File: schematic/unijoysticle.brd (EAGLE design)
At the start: 88.6 x 45.7 mm, 8 parts, among them CN1 DC JACK, IC1 4066N, IC2 4066N, IC3 4066N, J1 DB9, J2 DB9

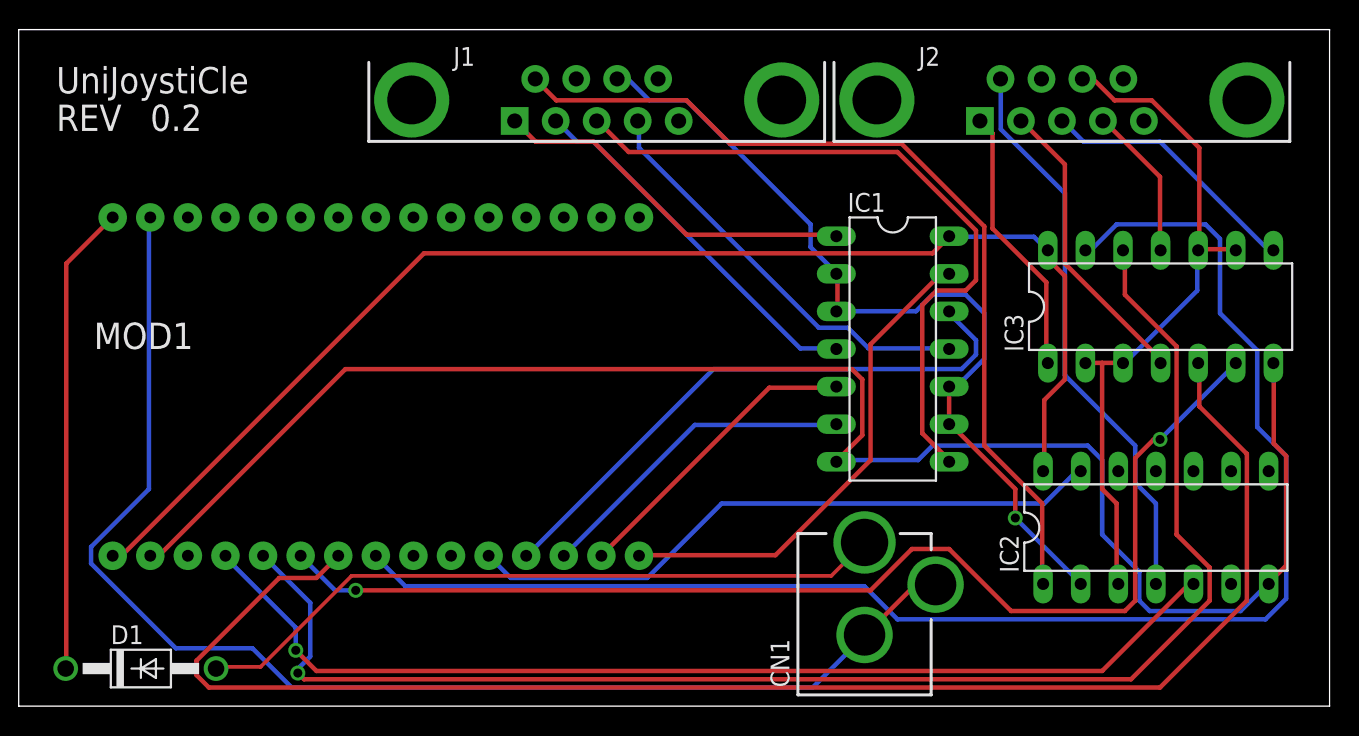
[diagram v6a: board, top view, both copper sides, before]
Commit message: fix: esp8622 schematic: ics with joy power. new dc jack barrel
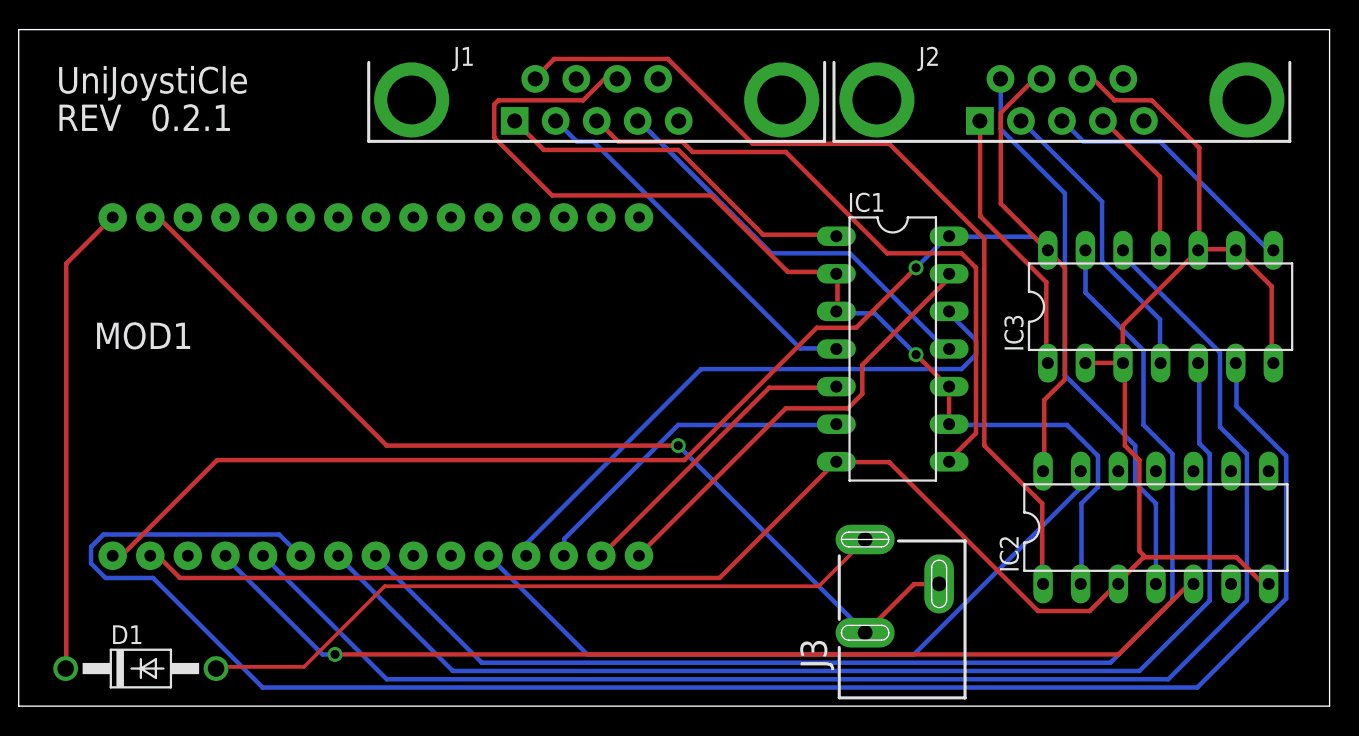
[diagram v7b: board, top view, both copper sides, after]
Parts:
- removed CN1: DC JACK, adafruit:DCJACK_2MM_PTH
- added J3: POWER_JACKSLT, SparkFun-Connectors:POWER_JACK_SLOT
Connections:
- removed net N$18: IC2.3, IC3.10, IC3.2, IC3.3, IC3.9, J2.8
- net 3.3V: now also J3.GND@1, J3.GND@2; no longer CN1.GND, CN1.GNDBREAK
- net GND: now also IC2.3, IC3.10, IC3.2, IC3.3, IC3.9, J2.8
- net N$23: now also J3.PWR; no longer CN1.PWR
- net VCC: now also J2.7
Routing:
- net N$18: track 47.1 -> 0.00 mm
- net J2LEFT: track 79.6 -> 120.2 mm, vias 2 -> 0
- net GND: track 114.8 -> 140.0 mm
- net J2DOWN: track 104.6 -> 80.4 mm
- net 3.3V: track 88.5 -> 66.3 mm, vias 0 -> 1
- net J2UP: track 100.3 -> 84.7 mm
- net N$2: track 58.1 -> 73.2 mm
- net VCC: track 88.6 -> 102.8 mm, vias 0 -> 1
- net J1FIRE: track 43.6 -> 48.6 mm
- net N$11: track 47.7 -> 43.6 mm
- net J1UP: track 33.5 -> 30.2 mm
- net J2FIRE: track 72.0 -> 70.2 mm
- net N$12: track 28.5 -> 27.4 mm
- net J1LEFT: track 22.1 -> 22.7 mm
- net N$21: track 60.3 -> 60.9 mm
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
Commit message: fix: joy pin #8 are connected
Not really needed since they are already connected inside the C64,
but usuful to have them connected in the board
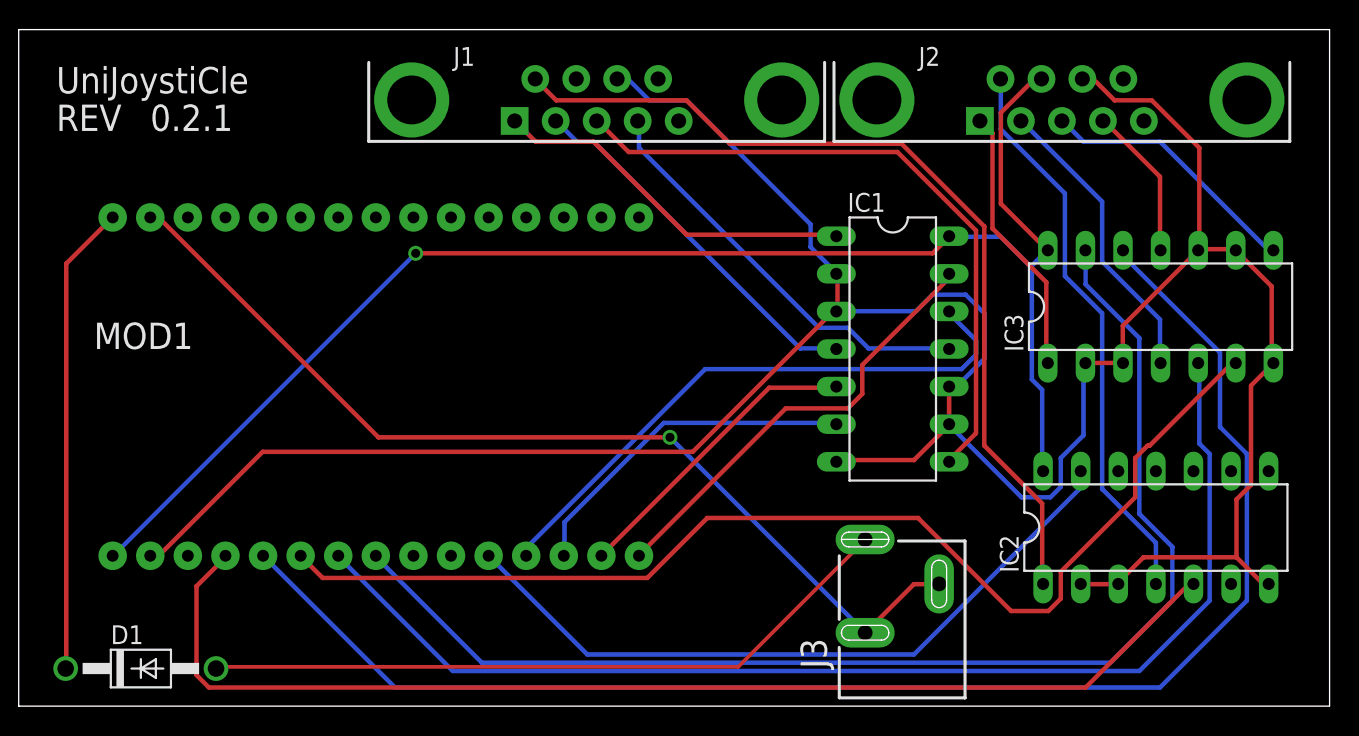
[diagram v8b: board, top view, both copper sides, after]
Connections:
- removed net N$2: IC1.10, IC1.2, IC1.3, IC1.9, IC2.2, J1.8
- net GND: now also IC1.10, IC1.2, IC1.3, IC1.9, IC2.2, J1.8
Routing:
- net N$2: track 73.2 -> 0.00 mm, vias 1 -> 0
- net GND: track 140.0 -> 193.5 mm
- net J2LEFT: track 120.2 -> 77.7 mm
- net J2FIRE: track 70.2 -> 79.5 mm, vias 1 -> 0
- net N$11: track 43.6 -> 45.1 mm
- net N$12: track 27.4 -> 28.5 mm
- net VCC: track 102.8 -> 101.9 mm
- net J1LEFT: track 22.7 -> 23.5 mm
- net N$21: track 60.9 -> 60.3 mm
